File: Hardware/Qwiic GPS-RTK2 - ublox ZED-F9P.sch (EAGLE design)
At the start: 58 parts, among them J1 Radio, J13 U.FL, J3 PTH, U2 3.3V, U3 ZED-F9P

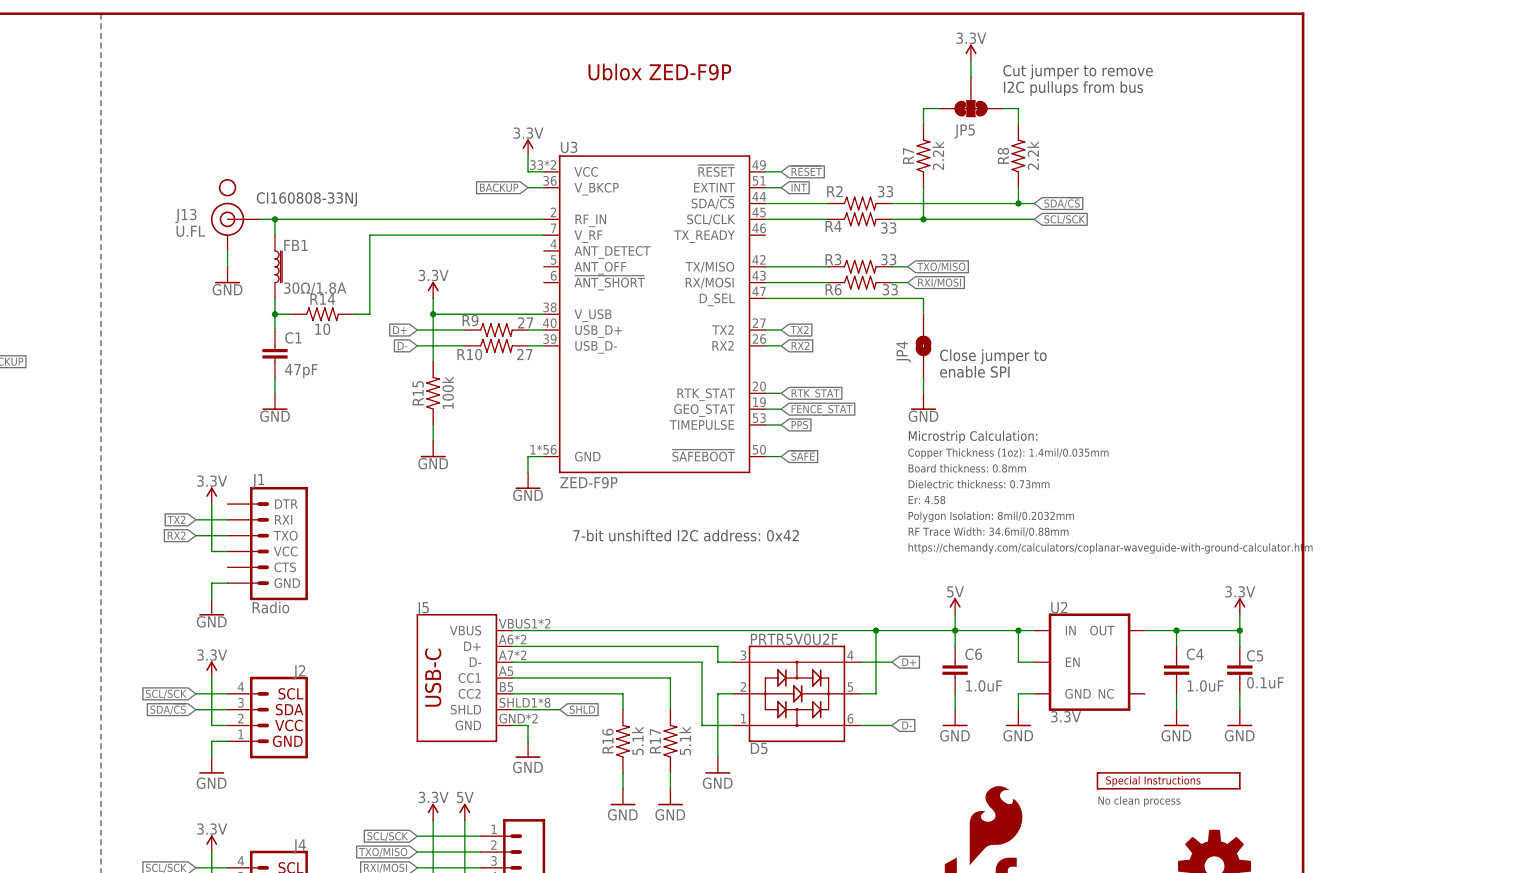
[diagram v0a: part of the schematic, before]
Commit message: v11 hardware: Added add' decoupling to USB VBUS, recomended induc to ant, more 33 ohm resistors.
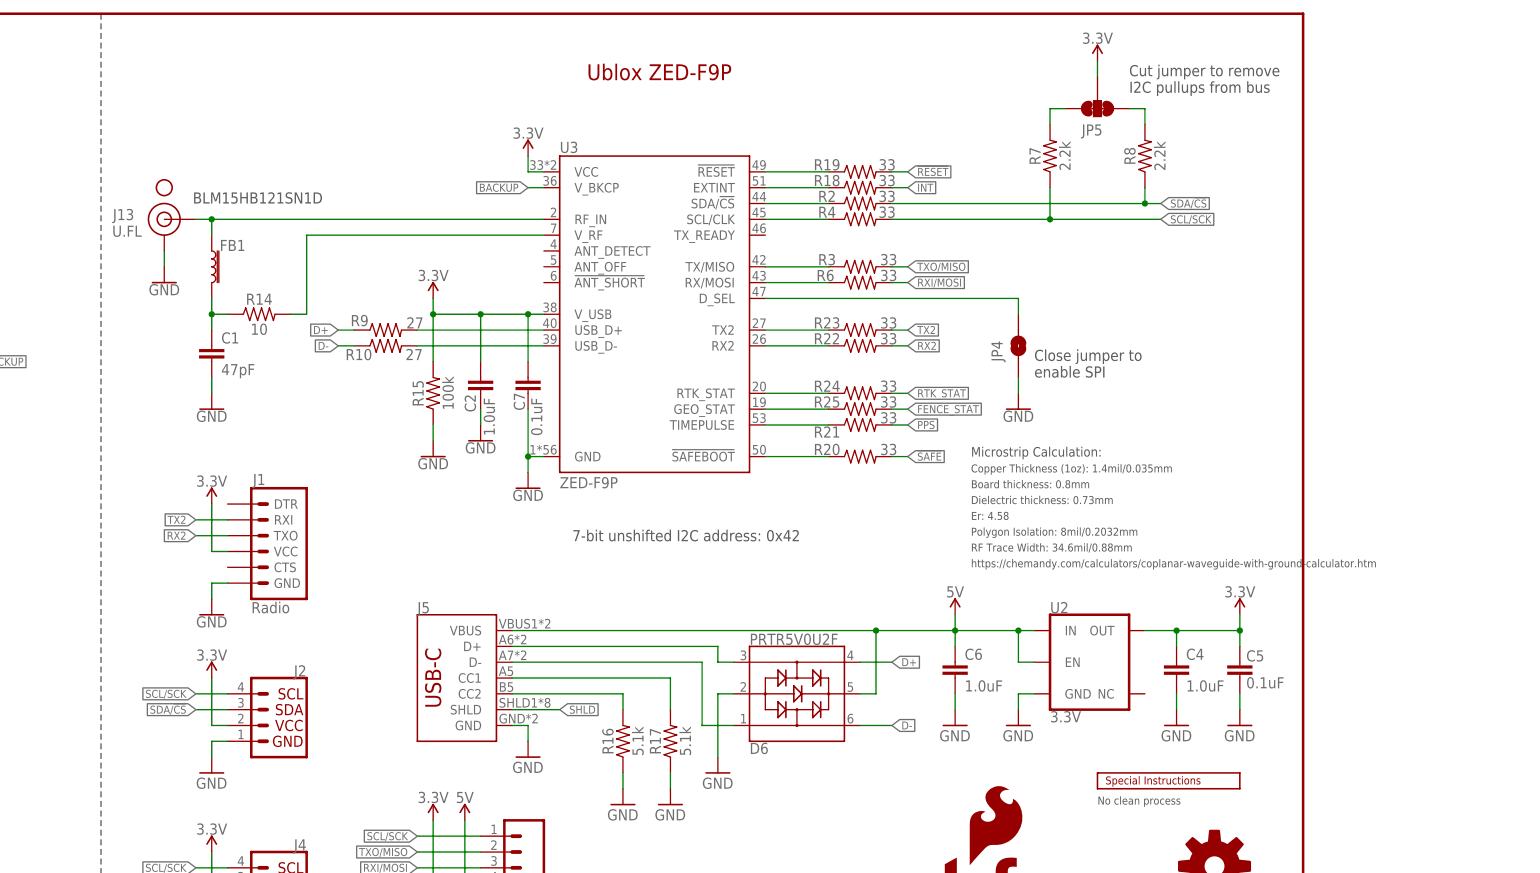
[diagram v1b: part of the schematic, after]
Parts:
- removed D5: PRTR5V0U2F, funbit:PRTR5V0U2F
- added C2: 1.0uF, SparkFun-Capacitors:1.0UF-0603-16V-10%
- added C7: 0.1uF, SparkFun-Capacitors:0.1UF-0603-25V-(+80/-20%)
- added D6: PRTR5V0U2F, SparkFun-IC-Power:PRTR5V0U2F
- added R18, R19, R20, R21, R22, R23, R24, R25: 33, SparkFun-Resistors:33OHM-0603-1/10W-1%
- FB1: value 30Ω/1.8A -> FERRITE_BEAD-120_OHM-0402; device SparkFun-Coils:FERRITE_BEAD-0603 -> SparkFun-Coils:FERRITE_BEAD-120_OHM-0402
- J5: device USB-C:USB_C16PIN -> SparkFun-Connectors:USB_C16PIN
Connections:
- new net N$14: R22.1, U3.RX2
- new net N$15: R18.1, U3.EXTINT
- new net N$16: R19.1, U3.!RESET!
- new net N$17: R21.1, U3.TIMEPULSE
- new net N$18: R20.1, U3.!SAFEBOOT!
- new net N$19: R24.1, U3.RTK_STAT
- new net N$20: R25.1, U3.GEO_STAT
- new net TX2_P: R23.1, U3.TX2
- net !RESET: now also R19.2; no longer U3.!RESET!
- net !SAFE: now also R20.2; no longer U3.!SAFEBOOT!
- net 3.3V: now also C2.1, C7.2
- net 5V: now also D6.5; no longer D5.5
- net D+: now also D6.4; no longer D5.4
- net D-: now also D6.6; no longer D5.6
- net FENCE_STAT: now also R25.2; no longer U3.GEO_STAT
- net GND: now also C2.2, C7.1, D6.2; no longer D5.2
- net INT: now also R18.2; no longer U3.EXTINT
- net PPS: now also R21.2; no longer U3.TIMEPULSE
- net RTK_STAT: now also R24.2; no longer U3.RTK_STAT
- net RX2: now also R22.2; no longer U3.RX2
- net TX2: now also R23.2; no longer U3.TX2
- net UNP_D+: now also D6.3; no longer D5.3
- net UNP_D-: now also D6.1; no longer D5.1
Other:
- note added: "BLM15HB121SN1D"
- note removed: "CI160808-33NJ"
- moved on the sheet: C1, FB1, J13, JP4, JP5, R10, R14, R7, R8, R9

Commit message: Adding readme, license, and gitignore.
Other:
- note added: "V11"
- note removed: "V10"
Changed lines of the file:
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@@
 <sheet>
 <plain>
-<text x="237.744" y="7.366" size="2.54" layer="94">V10</text>
+<text x="237.744" y="7.366" size="2.54" layer="94">V11</text>
 <text x="149.86" y="101.6" size="1.778" layer="97" align="center">7-bit unshifted I2C address: 0x42</text>
 <text x="145.542" y="176.022" size="2.54" layer="94" ratio="15" rot="MR180" align="center">Ublox ZED-F9P</text>
@@
 <text x="30.48" y="81.28" size="2.54" layer="94" ratio="15" rot="MR180" align="center">Stat LEDs</text>
 <wire x1="55.88" y1="185.42" x2="55.88" y2="0" width="0.1524" layer="97" style="longdash"/>
-<text x="220.98" y="172.72" size="1.778" layer="97">Cut jumper to remove
+<text x="184.658" y="172.72" size="1.778" layer="97">Cut jumper to remove
 I2C pullups from bus</text>
 <text x="19.558" y="73.914" size="1.778" layer="97">Cut jumper to
@@
 <text x="215.9" y="58.42" size="1.27" layer="97">No clean process</text>
 <text x="195.58" y="106.68" size="1.27" layer="97">Dielectric thickness: 0.73mm</text>
-<text x="195.58" y="96.52" size="1.27" layer="97">https://chemandy.com/calculators/coplanar-waveguide-with-ground-calculator.htm</text>
+<text x="195.58" y="96.52" size="0.762" layer="97">https://chemandy.com/calculators/coplanar-waveguide-with-ground-calculator.htm</text>
 <text x="195.58" y="114.3" size="1.524" layer="97" ratio="15">Microstrip Calculation:</text>
 </plain>

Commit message: Adding SMA connector to Antenna and SMA
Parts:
- removed J13: U.FL, SparkFun-Connectors:U.FL2PIN
- removed U$54: SMA-ANTENNA-THREADED, SparkFun-Hardware:SMA-ANTENNA-THREADED
- added E1, E2: SMA, SparkFun-RF:ANTENNA-GROUNDEDEDGE_SMA
- added PPS, PWR: JUMPER-SMT_2_NC_TRACE_SILK, SparkFun-Jumpers:JUMPER-SMT_2_NC_TRACE_SILK
- B1: device SparkFun-Batteries:BATTERY-6.8MM_SMD -> SparkFun-Batteries:ML414H_IV01E_BATTERY
- FB1: value FERRITE_BEAD-120_OHM-0402 -> 120_OHM
- J2, J4: value (none) -> Qwiic Right Angle
- J5: device SparkFun-Connectors:USB_C16PIN -> SparkFun-Connectors:USB_C_2-LAYER_PADS
- renumbered JP1 to PPS_LED, JP2 to RTK, JP3 to FENCE, JP4 to SPI
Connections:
- removed net SHLD: J5.SHLD
- new net N$21: PPS.1, R21.1
- new net PPS_STAT: J6.3, PPS_LED.2, R21.2
- net 3.3V: now also PWR.2; no longer R1.2
- net GND: now also E1.GND, E2.GND, J5.SHLD; no longer J13.GND
- net GPS_ANT1: now also E1.SIGNAL; no longer J13.SIGNAL
- net N$17: now also PWR.1, R1.2; no longer R21.1, U3.TIMEPULSE
- net PPS: now also E2.SIGNAL, PPS.2, U3.TIMEPULSE; no longer J6.3, PPS_LED.2, R21.2
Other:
- note added: "Board thickness: 1.6mm"
- note added: "Dielectric thickness (layer 1 to 2): 0.2mm"
- note added: "Er: 4.6"
- note added: "RF Trace Width: 13.8mil/0.35mm"
- note removed: "Board thickness: 0.8mm"
- note removed: "Dielectric thickness: 0.73mm"
- note removed: "Er: 4.58"
- note removed: "RF Trace Width: 34.6mil/0.88mm"
- moved on the sheet: C4, C5, C6, D6, R16, R17, R18, R19, R2, R20, R21, R22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

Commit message: Update caps to X7R. Change bead on RF input.
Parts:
- removed FRAME1: FRAME-LETTER, SparkFun-Aesthetics:FRAME-LETTER
- added FRAME2: FRAME-LEDGER, SparkFun-Aesthetics:FRAME-LEDGER
- C1: device SparkFun-Capacitors:47PF-0603-50V-5% -> SparkFun-Capacitors:47PF-0402-25V-5%-X7R
- C2, C3, C4, C6: device SparkFun-Capacitors:1.0UF-0603-16V-10% -> SparkFun-Capacitors:1.0UF-0603-16V-10%-X7R
- C5, C7: device SparkFun-Capacitors:0.1UF-0603-25V-(+80/-20%) -> SparkFun-Capacitors:0.1UF-0603-25V-5%
- FB1: value 120_OHM -> 120NH; device SparkFun-Coils:FERRITE_BEAD-120_OHM-0402 -> SparkFun-Coils:FERRITE_BEAD_GNSS
- R14: value 10 -> 33; device SparkFun-Resistors:10OHM-0603-1/10W-1% -> SparkFun-Resistors:33OHM-0603-1/10W-1%
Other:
- note added: "Connections"
- note added: "LQW15ANR12J00D"
- note added: "USB / Power"
- note added: "V12"
- note removed: "BLM15HB121SN1D"
- note removed: "V11"
- moved on the sheet: C1, C2, C4, C5, C6, C7, D1, D3, D4, D6, E1, E2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
